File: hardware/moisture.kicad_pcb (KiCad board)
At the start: 2 copper layers, 25 x 48 mm, 16 parts, among them P1 CON-SENSOR, P2 TST, P3 TST, Q1 S9013, U1 M24C64, U2 DRILL, U3 DRILL

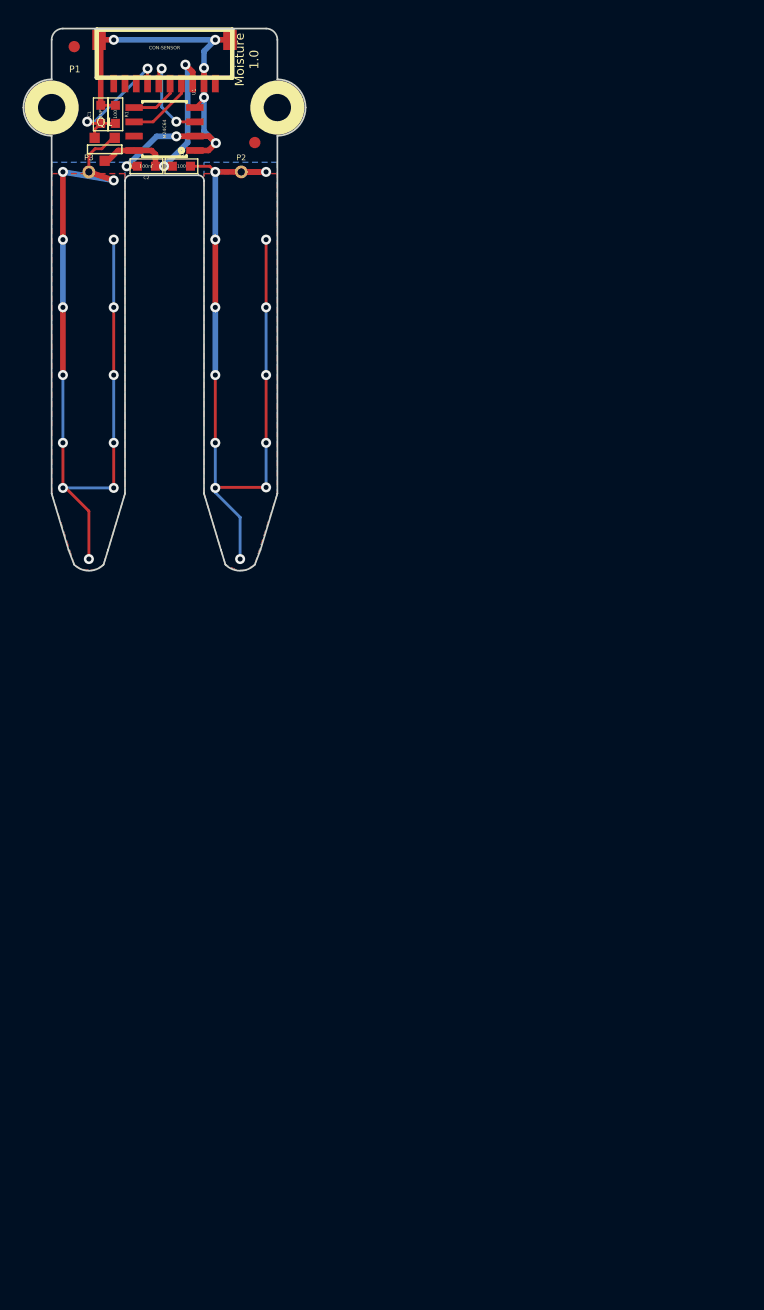
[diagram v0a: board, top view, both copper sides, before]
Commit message: remove not used prototypes, move to new hardware version
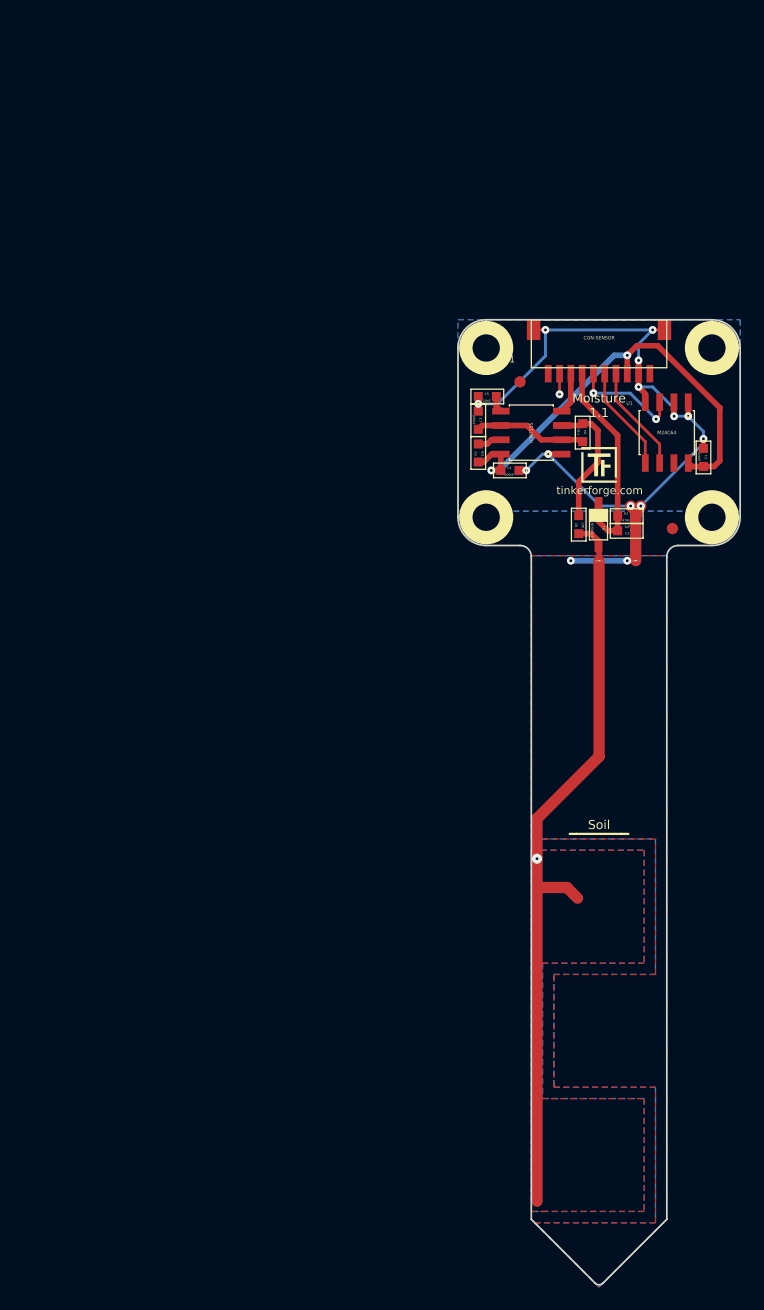
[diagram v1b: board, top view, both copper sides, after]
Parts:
- removed the Fiducial_Mark at (89.5, 42.9)
- removed the Fiducial_Mark at (105.5, 51.4)
- removed the G*** at (96.0, 48.3)
- removed Q1: S9013, SOT23EBC
- added C3: 100pF, kicad-libraries:0603, F.Cu at (125.3, 76.0)
- added C4: 100nF, kicad-libraries:0603, F.Cu at (128.1, 80.5)
- added C5: 10nF, kicad-libraries:0603, F.Cu at (126.1, 73.9)
- added D1: B0520LW, kicad-libraries:SOD-123, F.Cu at (135.9, 85.2)
- added Fiducial_Mark: VAL**, kicad-libraries:Fiducial_Mark, F.Cu at (129.0, 72.6)
- added Fiducial_Mark: VAL**, kicad-libraries:Fiducial_Mark, F.Cu at (142.5, 85.6)
- added G***: Logo_31x31, Logo_31x31, F.Cu at (134.4, 78.4)
- added R3: 10k, kicad-libraries:0603, F.Cu at (125.3, 78.9)
- added R4: 7.5k, kicad-libraries:0603, F.Cu at (134.6, 77.1)
- added U4: DRILL, kicad-libraries:DRILL_NP, F.Cu at (126.0, 69.6)
- added U5: DRILL, kicad-libraries:DRILL_NP, F.Cu at (146.0, 84.6)
- added U6: DRILL, kicad-libraries:DRILL_NP, F.Cu at (126.0, 84.6)
- C1: value DNP -> 100nF; footprint 0603 -> kicad-libraries:0603
- C2: value 100nF -> 1µF; footprint 0603 -> kicad-libraries:0603
- P1: footprint CON-SENSOR -> kicad-libraries:CON-SENSOR
- P2, P3: value TST -> CONN_1; footprint PINTST -> kicad-libraries:con
- R1: value 100 -> 470k; footprint 0603 -> kicad-libraries:0603
- R2: value 100 -> 4k7; footprint 0603 -> kicad-libraries:0603
- U1: footprint SOIC8 -> kicad-libraries:SOIC8
- U2: value DRILL -> ICM7555; footprint DRILL_NP -> kicad-libraries:SOIC8
- U3: footprint DRILL_NP -> kicad-libraries:DRILL_NP
- moved C1 61.4 mm to (145.2, 79.3)
- moved P3 59.4 mm to (139.2, 88.5)
- moved R1 57.6 mm to (138.4, 84.5), turned to 180 degrees
- moved VAL 56.2 mm to (136.1, 81.2)
- moved C2 53.4 mm to (138.4, 85.8), turned to 0 degrees
- moved U1 52.0 mm to (142.0, 77.1), turned to 180 degrees
- moved U2 51.3 mm to (130.0, 77.1), turned to 90 degrees
- moved R2 47.4 mm to (134.2, 85.2), turned to 270 degrees
- moved P2 46.8 mm to (136.0, 88.5)
- moved P1 46.3 mm to (136.0, 67.1)
- moved U3 44.0 mm to (146.0, 69.6)
- moved VAL 42.5 mm to (136.1, 72.2)
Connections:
- C1 pad 1: N-000003 -> VCC
- C2 pad 1: VCC -> Net-(C2-Pad1)
- P1 pad 1: N-0000013 -> (no net)
- P1 pad 10: N-000004 -> (no net)
- P1 pad 7: N-000003 -> Net-(C2-Pad1)
- P1 pad 8: N-000006 -> RESET
- P1 pad 9: N-000005 -> GND
- P3 pad 1: N-000002 -> GND
- R1 pad 2: N-000003 -> Net-(C2-Pad1)
- R2 pad 1: VCC -> CLK
- U1 pad 7: N-0000011 -> (no net)
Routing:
- net N-000002: track 73.2 -> 0.00 mm, vias 13 -> 0
- net GND: track 43.7 -> 77.4 mm, vias 7 -> 15
- net VCC: track 21.0 -> 41.2 mm
- net Net-(C2-Pad1): track 0.00 -> 18.9 mm
- net CLK: track 0.00 -> 13.3 mm
- net N-000003: track 12.7 -> 0.00 mm, vias 2 -> 0
- net Net-(C3-Pad1): track 0.00 -> 9.98 mm
- net Net-(P1-Pad5): track 4.59 -> 9.41 mm
- net Net-(D1-Pad1): track 70.8 -> 66.8 mm, vias 13 -> 1
- net RESET: track 0.00 -> 3.66 mm
- net Net-(P1-Pad4): track 6.12 -> 9.52 mm
- net Net-(R3-Pad1): track 0.00 -> 2.15 mm
- net Net-(P1-Pad6): track 8.32 -> 9.86 mm
- net Net-(C5-Pad1): track 0.00 -> 1.46 mm
- added copper zone on B.Cu, net GND
- added copper zone on F.Cu, net GND
- removed copper zone on B.Cu, net N-000002
- removed copper zone on F.Cu, net N-000002
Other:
- board size 25 x 48 mm -> 25 x 85.5 mm
- net class Default: clearance 0.254 -> 0.19; via_dia 0.889 -> 0.7; via_drill 0.635 -> 0.25
- rule trace_clearance: 0.254 -> 0.19
- rule via_min_drill: 0.508 -> 0.25
- rule via_min_size: 0.889 -> 0.7
- board text added: "Copyright Tinkerforge GmbH 2014. This documentation describes Open Hardware and is licensed under the CERN OHL v. 1.1. You may redistribute and modify this documentation under the terms of the CERN OHL v.1.1. (http://ohwr.org/cernohl). This documentation is distributed WITHOUT ANY EXPRESS OR IMPLIED WARRANTY, INCLUDING OF MERCHANTABILITY, SATISFACTORY QUALITY AND FITNESS FOR A PARTICULAR PURPOSE.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"
- board text added: "Moisture 1.1"
- board text added: "Soil"
- board text removed: "Copyright Tinkerforge GmbH 2013. This documentation describes Open Hardware and is licensed under the CERN OHL v. 1.1. You may redistribute and modify this documentation under the terms of the CERN OHL v.1.1. (http://ohwr.org/cernohl). This documentation is distributed WITHOUT ANY EXPRESS OR IMPLIED WARRANTY, INCLUDING OF MERCHANTABILITY, SATISFACTORY QUALITY AND FITNESS FOR A PARTICULAR PURPOSE.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"
- board text removed: "Moisture 1.0"

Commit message: Add 3d information (final)
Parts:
- C1, C2, C3, C4, C5: footprint kicad-libraries:0603 -> kicad-libraries:C0603
- G***: footprint Logo_31x31 -> kicad-libraries:Logo_31x31
- R1, R2, R3, R4: footprint kicad-libraries:0603 -> kicad-libraries:R0603
- VAL: footprint CE_5mm -> kicad-libraries:CE_5mm
- VAL: footprint WEEE_7mm -> kicad-libraries:WEEE_7mm
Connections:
- P1 pad 1: (no net) -> Net-(P1-Pad1)
- P1 pad 10: (no net) -> Net-(P1-Pad10)
- U1 pad 7: (no net) -> Net-(U1-Pad7)
